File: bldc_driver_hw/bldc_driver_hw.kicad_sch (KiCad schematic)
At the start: 28 parts, among them J1 Conn_01x02, J10 MR60_F, J2 USB_C_Receptacle_USB2.0_16P, J3 JTAG_CONN, J4 USB_C_Receptacle_USB2.0_16P, J5 Conn_01x03_Pin, J6 Conn_01x03_Pin, J7 Conn_01x03, J9 Conn_01x02, U2 USBLC6-2SC6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

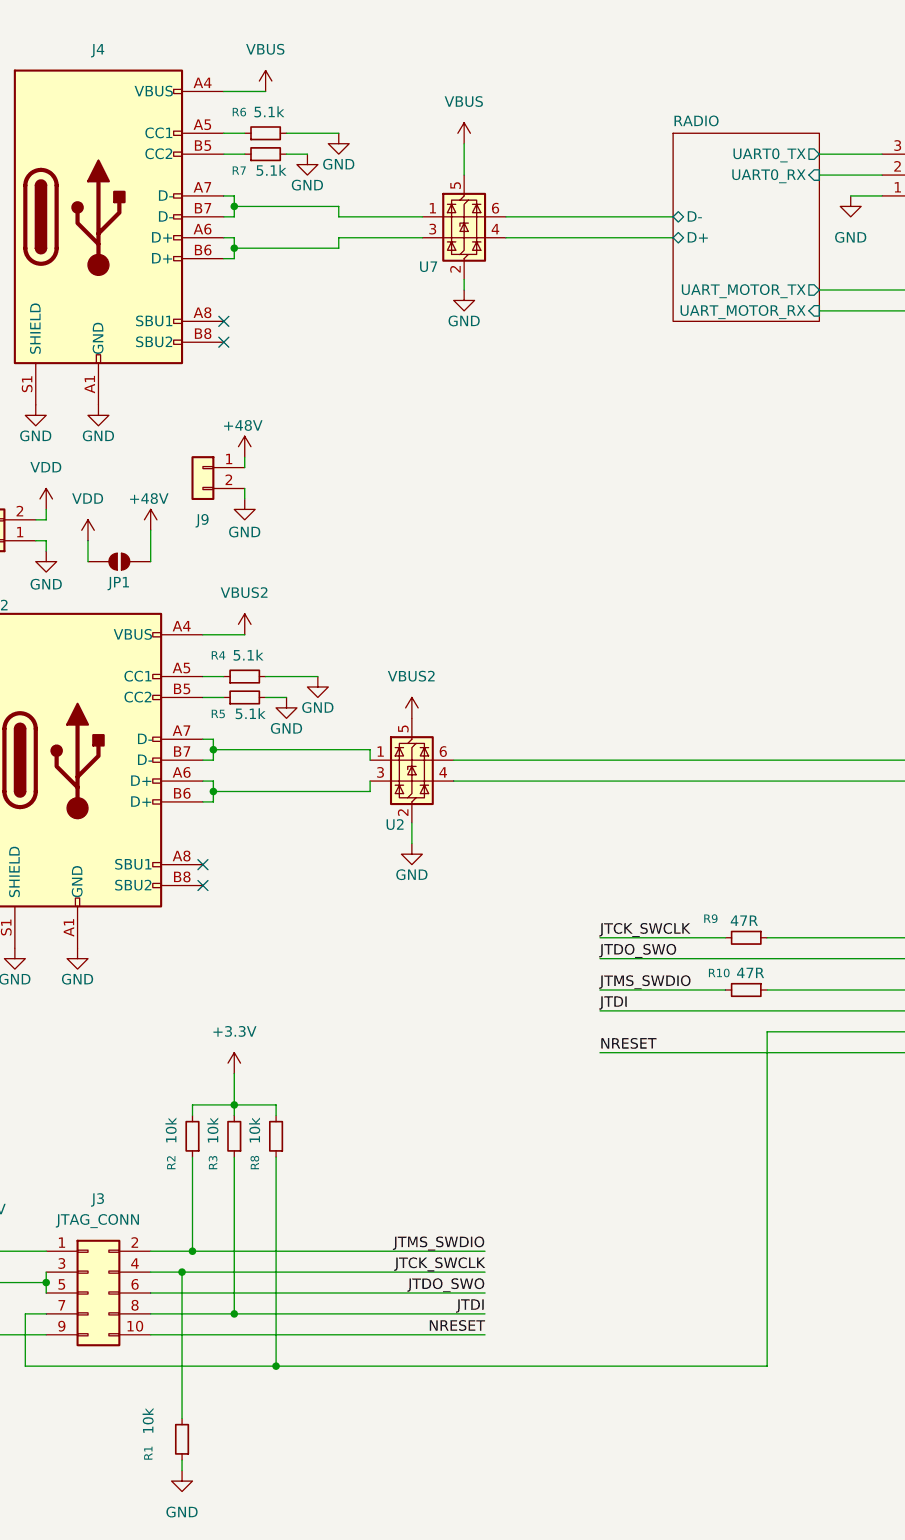
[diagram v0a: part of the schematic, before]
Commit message: added lcsc codes
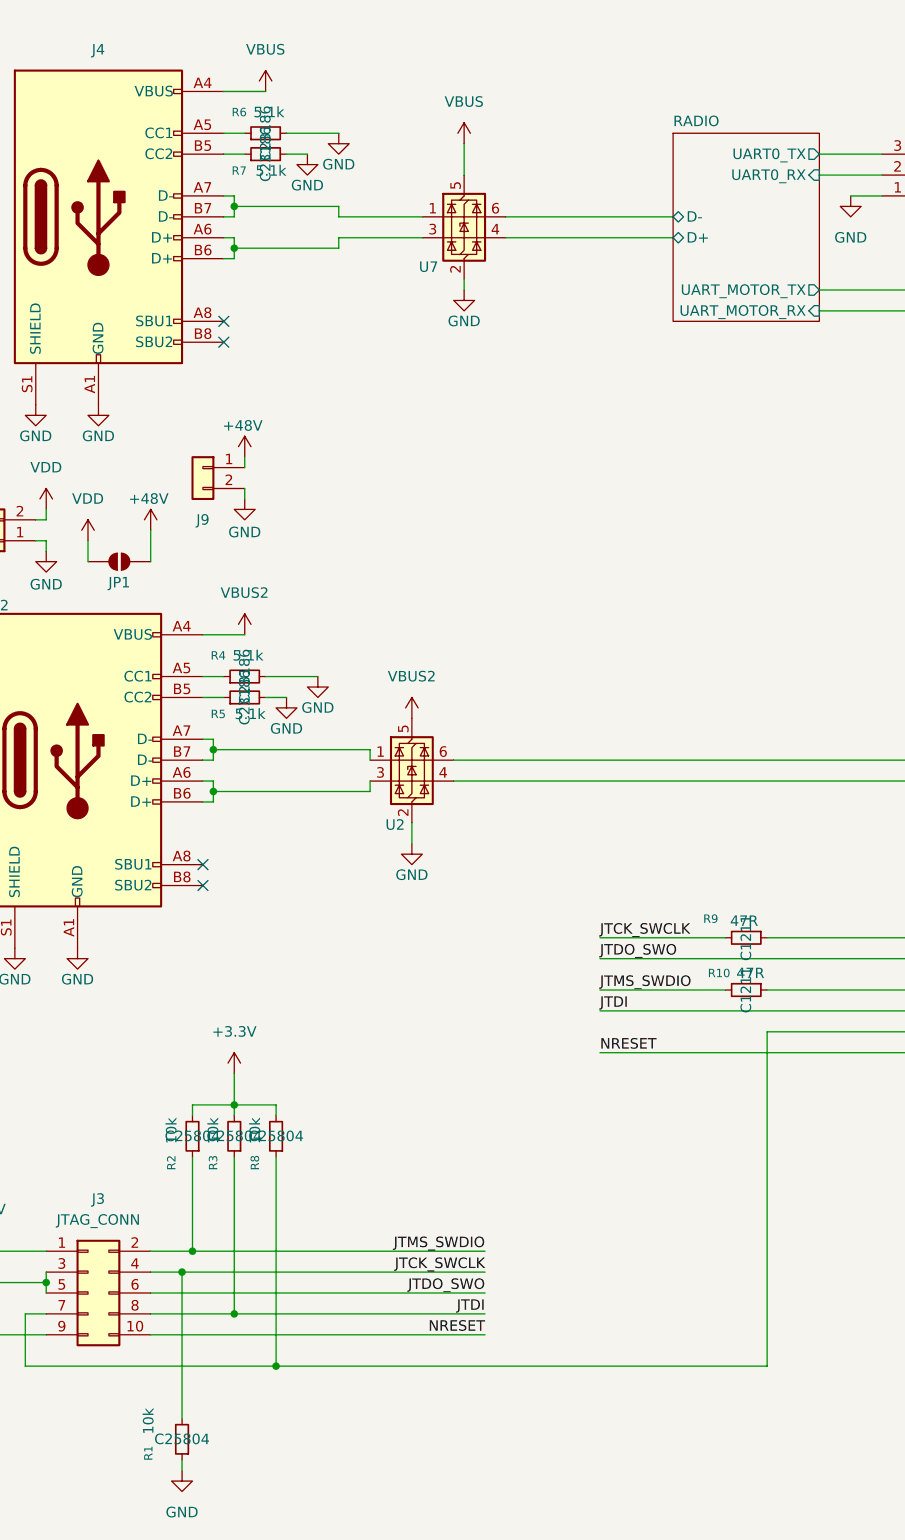
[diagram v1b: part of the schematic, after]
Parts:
- R1, R2, R3, R8: LCSC (none) -> C25804
- R10, R9: LCSC (none) -> C1211
- R4, R5, R6, R7: LCSC (none) -> C23186

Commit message: finished_board
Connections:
- net MCU/JTRST is gone; now on net JTCK_SWCLK: J3.7 (Pin_7), R8.1
- net CAN_TRANSCIEVER/CAN_H: now also J7.3 (Pin_3); no longer J7.2 (Pin_2)
- net CAN_TRANSCIEVER/CAN_L: now also J7.2 (Pin_2); no longer J7.1 (Pin_1)
- net GND: now also J7.1 (Pin_1); no longer J7.3 (Pin_3)
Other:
- note added: "CAN ENDPOINT"
- note added: "JTAG"
- note added: "POWER_CONNECTORS"
- note added: "RADIO USB_ENDPOINT"
- note added: "STM32 USB_ENDPOINT"
- moved on the sheet: H1, H2, H3, H4, H5, H6, J1, J3, J6, J9, JP1, R1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

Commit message: finished
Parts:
- J1, J10, J2, J3, J4, J5, J6, J7, J9, U2, U7: now left out of the parts list
- R10, R9: LCSC C1211 -> C23182
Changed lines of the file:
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@@
 		(unit 1)
 		(exclude_from_sim no)
-		(in_bom yes)
+		(in_bom no)
 		(on_board yes)
 		(dnp no)
@@
 			)
 		)
-		(property "LCSC" "C1211"
+		(property "LCSC" "C23182"
 			(at 130.81 132.08 0)
 			(effects
@@
 		(unit 1)
 		(exclude_from_sim no)
-		(in_bom yes)
+		(in_bom no)
 		(on_board yes)
 		(dnp no)
@@
 		(unit 1)
 		(exclude_from_sim no)
-		(in_bom yes)
+		(in_bom no)
 		(on_board yes)
 		(dnp no)
@@
 		(unit 1)
 		(exclude_from_sim no)
-		(in_bom yes)
+		(in_bom no)
 		(on_board yes)
 		(dnp no)
@@
 		(unit 1)
 		(exclude_from_sim no)
-		(in_bom yes)
+		(in_bom no)
 		(on_board yes)
 		(dnp no)
@@
 		(unit 1)
 		(exclude_from_sim no)
-		(in_bom yes)
+		(in_bom no)
 		(on_board yes)
 		(dnp no)
@@
 		(unit 1)
 		(exclude_from_sim no)
-		(in_bom yes)
+		(in_bom no)
 		(on_board yes)
 		(dnp no)
@@
 		(unit 1)
 		(exclude_from_sim no)
-		(in_bom yes)
+		(in_bom no)
 		(on_board yes)
 		(dnp no)
@@
 		(unit 1)
 		(exclude_from_sim no)
-		(in_bom yes)
+		(in_bom no)
 		(on_board yes)
 		(dnp no)
@@
 		(unit 1)
 		(exclude_from_sim no)
-		(in_bom yes)
+		(in_bom no)
 		(on_board yes)
 		(dnp no)
@@
 			)
 		)
-		(property "LCSC" "C1211"
+		(property "LCSC" "C23182"
 			(at 130.81 125.73 0)
 			(effects
@@
 		(unit 1)
 		(exclude_from_sim no)
-		(in_bom yes)
+		(in_bom no)
 		(on_board yes)
 		(dnp no)

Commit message: Changed size of capacitors at input 48V dc converter
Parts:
- R4, R5, R6, R7: footprint Capacitor_SMD:C_0603_1608Metric -> Resistor_SMD:R_0603_1608Metric
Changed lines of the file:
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@@
 			)
 		)
-		(property "Footprint" "Capacitor_SMD:C_0603_1608Metric"
+		(property "Footprint" "Resistor_SMD:R_0603_1608Metric"
 			(at 52.07 30.48 0)
 			(effects
@@
 			)
 		)
-		(property "Footprint" "Capacitor_SMD:C_0603_1608Metric"
+		(property "Footprint" "Resistor_SMD:R_0603_1608Metric"
 			(at 52.07 27.94 0)
 			(effects
@@
 			)
 		)
-		(property "Footprint" "Capacitor_SMD:C_0603_1608Metric"
+		(property "Footprint" "Resistor_SMD:R_0603_1608Metric"
 			(at 49.53 93.98 0)
 			(effects
@@
 			)
 		)
-		(property "Footprint" "Capacitor_SMD:C_0603_1608Metric"
+		(property "Footprint" "Resistor_SMD:R_0603_1608Metric"
 			(at 49.53 96.52 0)
 			(effects

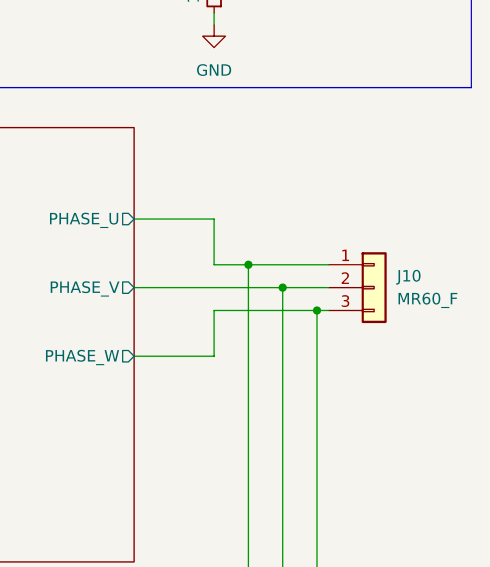
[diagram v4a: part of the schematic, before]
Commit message: changed vref
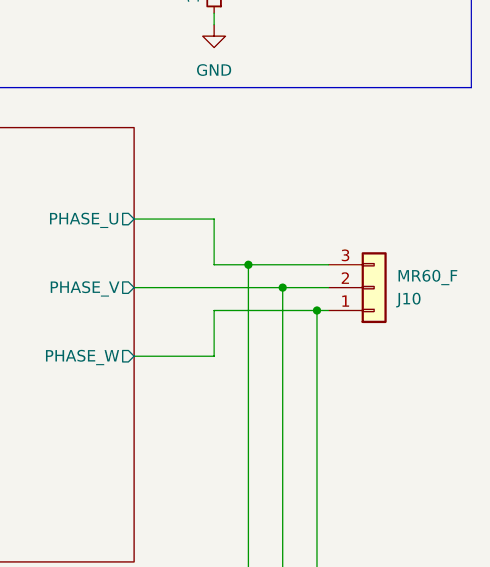
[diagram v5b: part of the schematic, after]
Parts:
- J10: footprint bldc_driver_footprint:MR60-F -> Connector_Phoenix_GMSTB:PhoenixContact_GMSTBVA_2,5_3-G_1x03_P7.50mm_Vertical
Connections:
- net BEMF_SENS/PHASE_U: now also J10.3 (Pin_3); no longer J10.1 (Pin_1)
- net BEMF_SENS/PHASE_W: now also J10.1 (Pin_1); no longer J10.3 (Pin_3)
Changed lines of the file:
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@@
 		(lib_id "Connector_Generic:Conn_01x03")
 		(at 273.05 97.79 0)
+		(mirror x)
 		(unit 1)
 		(exclude_from_sim no)
@@
 		(on_board yes)
 		(dnp no)
-		(fields_autoplaced yes)
 		(property "Reference" "J10"
-			(at 275.59 96.5199 0)
+			(at 275.59 99.0601 0)
 			(effects
 				(font
@@
 		)
 		(property "Value" "MR60_F"
-			(at 275.59 99.0599 0)
+			(at 275.59 96.5201 0)
 			(effects
 				(font
@@
 			)
 		)
-		(property "Footprint" "bldc_driver_footprint:MR60-F"
+		(property "Footprint" "Connector_Phoenix_GMSTB:PhoenixContact_GMSTBVA_2,5_3-G_1x03_P7.50mm_Vertical"
 			(at 273.05 97.79 0)
 			(effects
